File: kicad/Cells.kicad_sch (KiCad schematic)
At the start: 48 parts

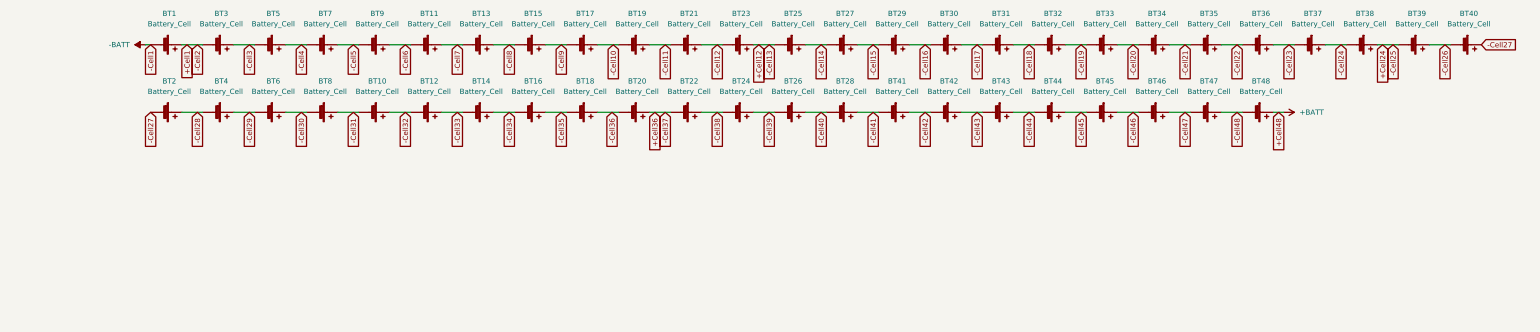
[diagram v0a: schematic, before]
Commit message: fixed cell layout, started making balancing circuitry
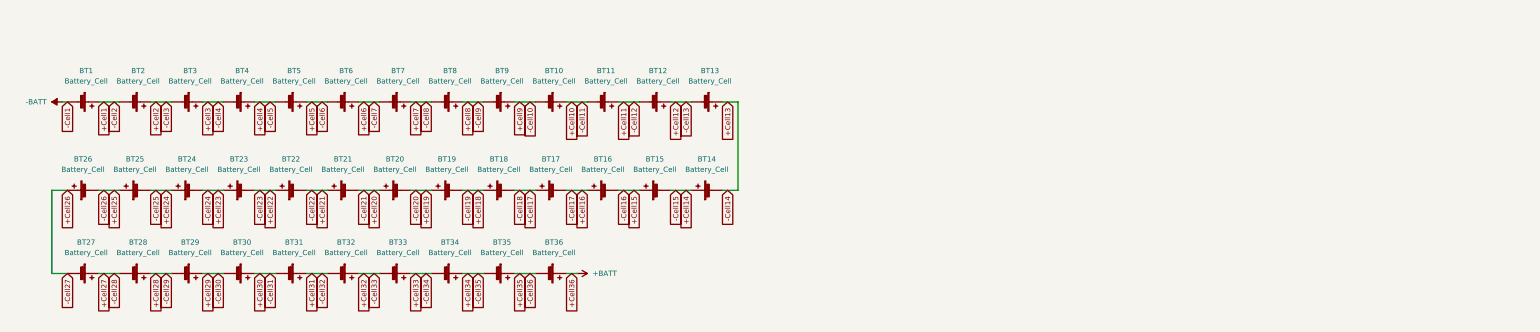
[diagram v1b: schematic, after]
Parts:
- removed BT22, BT24, BT26, BT28, BT41, BT42, BT43, BT44, BT45, BT46, BT47, BT48: Battery_Cell, symbol Device:Battery_Cell
- renumbered BT19 to BT10, BT21 to BT11, BT23 to BT12, BT25 to BT13, BT27 to BT14, BT29 to BT15, BT30 to BT16, BT31 to BT17, BT32 to BT18, BT33 to BT19, BT3 to BT2, BT34 to BT20, BT35 to BT21, BT36 to BT22, BT37 to BT23, BT38 to BT24, BT39 to BT25, BT40 to BT26, BT2 to BT27, BT4 to BT28, BT6 to BT29, BT5 to BT3, BT8 to BT30, BT10 to BT31, BT12 to BT32, BT14 to BT33, BT16 to BT34, BT18 to BT35, BT20 to BT36, BT7 to BT4, BT9 to BT5, BT11 to BT6, BT13 to BT7, BT15 to BT8, BT17 to BT9
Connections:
- net +Cell36 is gone; now on net +BATT: BT36.1 (+)
- net -Cell10 renamed +Cell9
- net -Cell11 renamed +Cell10
- net -Cell12 renamed +Cell11
- net -Cell14 renamed +Cell13
- net -Cell15 renamed +Cell14
- net -Cell16 renamed +Cell15
- net -Cell17 renamed +Cell16
- net -Cell18 renamed +Cell17
- net -Cell19 renamed +Cell18
- net -Cell20 renamed +Cell19
- net -Cell21 renamed +Cell20
- net -Cell22 renamed +Cell21
- net -Cell23 renamed +Cell22
- net -Cell24 renamed +Cell23
- net -Cell26 renamed +Cell25
- net -Cell27 renamed +Cell26
- net -Cell28 renamed +Cell27
- net -Cell29 renamed +Cell28
- net -Cell3 renamed +Cell2
- net -Cell30 renamed +Cell29
- net -Cell31 renamed +Cell30
- net -Cell32 renamed +Cell31
- net -Cell33 renamed +Cell32
- net -Cell34 renamed +Cell33
- net -Cell35 renamed +Cell34
- net -Cell36 renamed +Cell35
- net -Cell4 renamed +Cell3
- net -Cell5 renamed +Cell4
- net -Cell6 renamed +Cell5
- net -Cell7 renamed +Cell6
- net -Cell8 renamed +Cell7
- net -Cell9 renamed +Cell8
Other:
- title: Power -> Cells
- moved on the sheet: BT1, BT10, BT11, BT12, BT13, BT14, BT15, BT16, BT17, BT18, BT19, BT2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

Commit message: Added charge MOSFET
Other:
- moved on the sheet: BT1, BT10, BT11, BT12, BT13, BT14, BT15, BT16, BT17, BT18, BT19, BT2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
